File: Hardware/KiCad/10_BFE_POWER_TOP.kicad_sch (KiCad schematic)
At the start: 0 parts

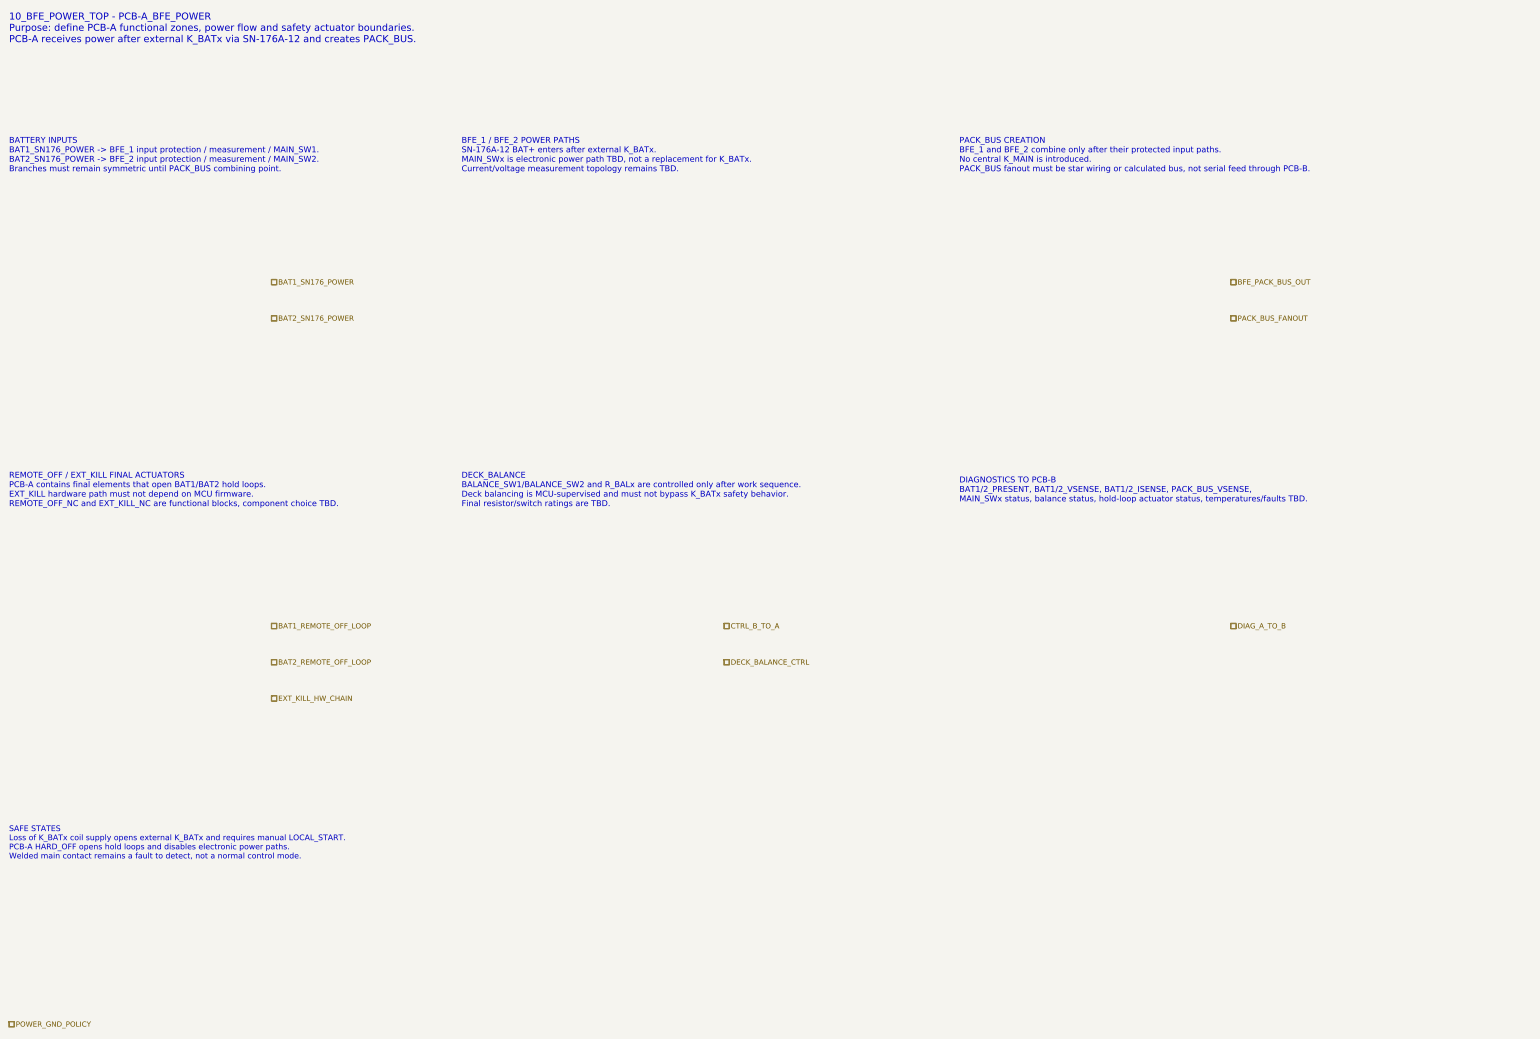
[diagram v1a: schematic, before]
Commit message: hardware: add BFE detailed hierarchy sheets
Add Architecture Level A detailed hierarchy sheets for PCB-A BFE_POWER.

Includes 11_BATTERY_INPUT_1 through 19_BFE_CONNECTORS_TESTPOINTS and updates the BFE top sheet/manifest.

No component selection, footprints, PCB layout, K_MAIN, or .kicad_prl changes.
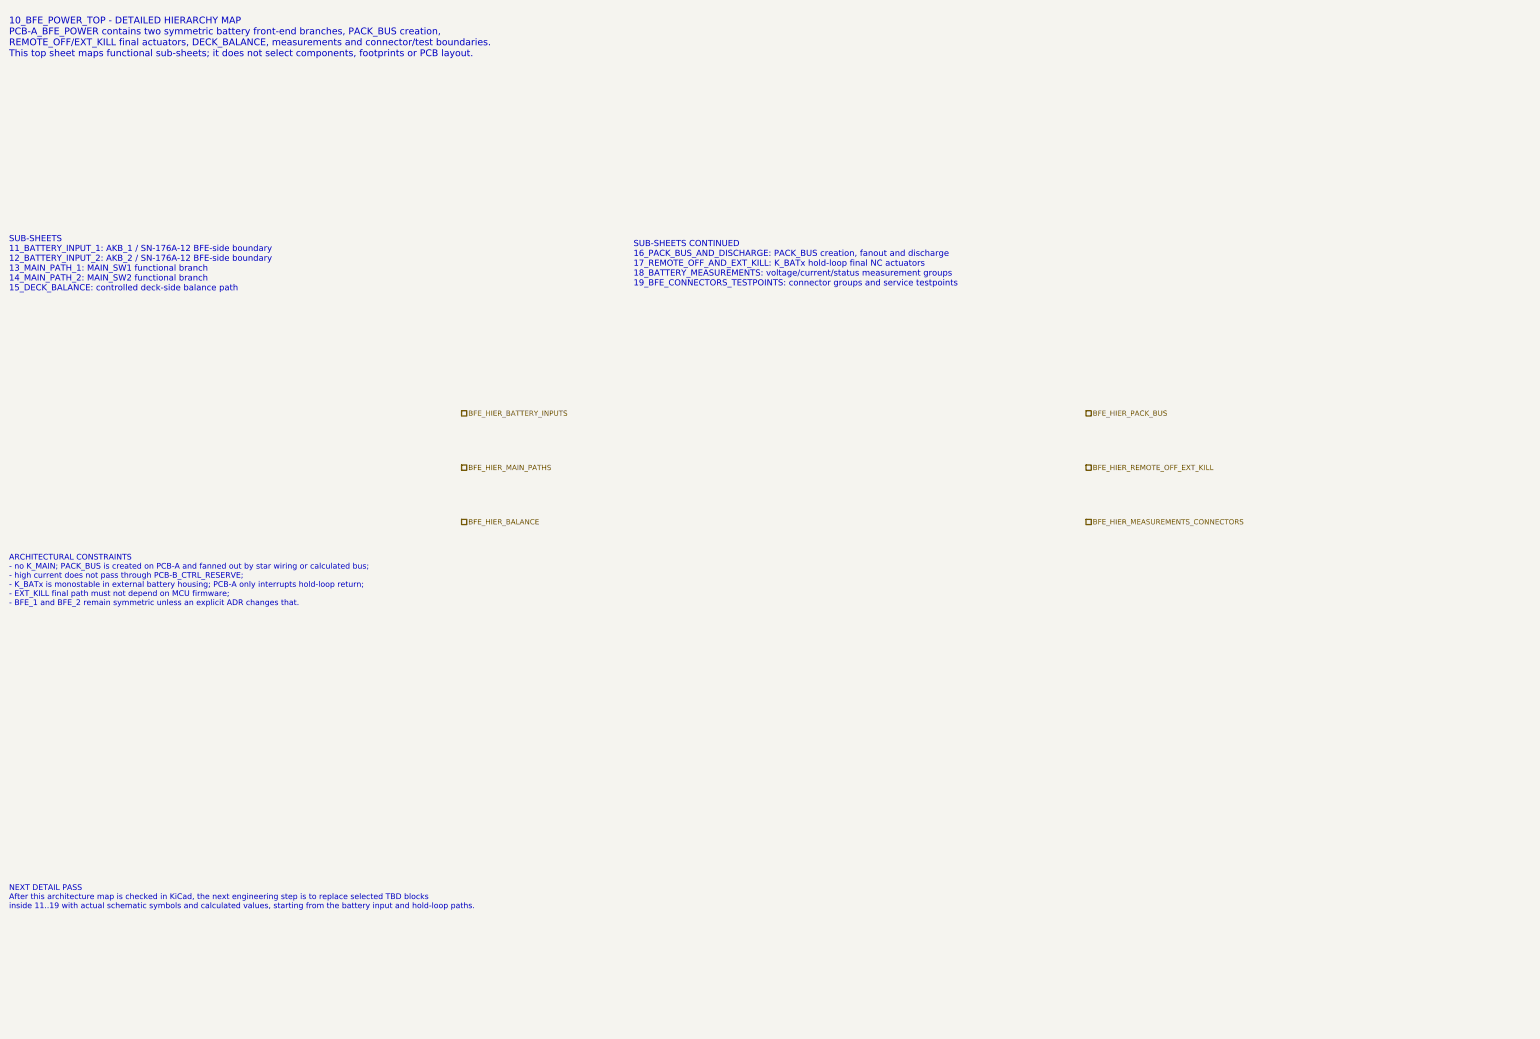
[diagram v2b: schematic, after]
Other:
- note added: "10_BFE_POWER_TOP - DETAILED HIERARCHY MAP PCB-A_BFE_POWER contains two symmetric battery front-end branches, PACK_BUS creation, REMOTE_OFF/EXT_KILL final actuators, DECK_BALANCE, measurements and connector/test boundaries. This top sheet maps functional sub-sheets; it does not select components, footprints or PCB layout."
- note added: "ARCHITECTURAL CONSTRAINTS - no K_MAIN; PACK_BUS is created on PCB-A and fanned out by star wiring or calculated bus; - high current does not pass through PCB-B_CTRL_RESERVE; - K_BATx is monostable in external battery housing; PCB-A only interrupts hold-loop return; - EXT_KILL final path must not depend on MCU firmware; - BFE_1 and BFE_2 remain symmetric unless an explicit ADR changes that."
- note added: "NEXT DETAIL PASS After this architecture map is checked in KiCad, the next engineering step is to replace selected TBD blocks inside 11..19 with actual schematic symbols and calculated values, starting from the battery input and hold-loop paths."
- note added: "SUB-SHEETS 11_BATTERY_INPUT_1: AKB_1 / SN-176A-12 BFE-side boundary 12_BATTERY_INPUT_2: AKB_2 / SN-176A-12 BFE-side boundary 13_MAIN_PATH_1: MAIN_SW1 functional branch 14_MAIN_PATH_2: MAIN_SW2 functional branch 15_DECK_BALANCE: controlled deck-side balance path"
- note added: "SUB-SHEETS CONTINUED 16_PACK_BUS_AND_DISCHARGE: PACK_BUS creation, fanout and discharge 17_REMOTE_OFF_AND_EXT_KILL: K_BATx hold-loop final NC actuators 18_BATTERY_MEASUREMENTS: voltage/current/status measurement groups 19_BFE_CONNECTORS_TESTPOINTS: connector groups and service testpoints"
- note removed: "10_BFE_POWER_TOP - PCB-A_BFE_POWER Purpose: define PCB-A functional zones, power flow and safety actuator boundaries. PCB-A receives power after external K_BATx via SN-176A-12 and creates PACK_BUS."
- note removed: "BATTERY INPUTS BAT1_SN176_POWER -> BFE_1 input protection / measurement / MAIN_SW1. BAT2_SN176_POWER -> BFE_2 input protection / measurement / MAIN_SW2. Branches must remain symmetric until PACK_BUS combining point."
- note removed: "BFE_1 / BFE_2 POWER PATHS SN-176A-12 BAT+ enters after external K_BATx. MAIN_SWx is electronic power path TBD, not a replacement for K_BATx. Current/voltage measurement topology remains TBD."
- note removed: "DECK_BALANCE BALANCE_SW1/BALANCE_SW2 and R_BALx are controlled only after work sequence. Deck balancing is MCU-supervised and must not bypass K_BATx safety behavior. Final resistor/switch ratings are TBD."
- note removed: "DIAGNOSTICS TO PCB-B BAT1/2_PRESENT, BAT1/2_VSENSE, BAT1/2_ISENSE, PACK_BUS_VSENSE, MAIN_SWx status, balance status, hold-loop actuator status, temperatures/faults TBD."
- note removed: "PACK_BUS CREATION BFE_1 and BFE_2 combine only after their protected input paths. No central K_MAIN is introduced. PACK_BUS fanout must be star wiring or calculated bus, not serial feed through PCB-B."
- note removed: "REMOTE_OFF / EXT_KILL FINAL ACTUATORS PCB-A contains final elements that open BAT1/BAT2 hold loops. EXT_KILL hardware path must not depend on MCU firmware. REMOTE_OFF_NC and EXT_KILL_NC are functional blocks, component choice TBD."
- note removed: "SAFE STATES Loss of K_BATx coil supply opens external K_BATx and requires manual LOCAL_START. PCB-A HARD_OFF opens hold loops and disables electronic power paths. Welded main contact remains a fault to detect, not a normal control mode."
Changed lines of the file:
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@@
 		(title "10_BFE_POWER_TOP - PCB-A_BFE_POWER")
 		(date "2026-07-15")
-		(rev "A1")
+		(rev "A2")
 		(company "Gonoboben/plataVM")
-		(comment 1 "Architecture Level A: BFE branches, PACK_BUS and final HARD_OFF actuators")
-		(comment 2 "No K_BATx/MAIN_SWx/current sensor part numbers selected")
+		(comment 1 "Architecture Level A: BFE detailed hierarchy map")
+		(comment 2 "Sub-sheets 11..19 define functional boundaries only")
 	)
-	(text "10_BFE_POWER_TOP - PCB-A_BFE_POWER\nPurpose: define PCB-A functional zones, power flow and safety actuator boundaries.\nPCB-A receives power after external K_BATx via SN-176A-12 and creates PACK_BUS."
+	(text "10_BFE_POWER_TOP - DETAILED HIERARCHY MAP\nPCB-A_BFE_POWER contains two symmetric battery front-end branches, PACK_BUS creation,\nREMOTE_OFF/EXT_KILL final actuators, DECK_BALANCE, measurements and connector/test boundaries.\nThis top sheet maps functional sub-sheets; it does not select components, footprints or PCB layout."
 		(exclude_from_sim no)
-		(at 12 10 0)
-		(effects (font (size 1.55 1.55)) (justify left))
-		(uuid "bfe-a-text-0001")
+		(at 12 12 0)
+		(effects (font (size 1.5 1.5)) (justify left))
+		(uuid "bfe-top-00000010-0000-4000-8000-000000000101")
 	)
-	(text "BATTERY INPUTS\nBAT1_SN176_POWER -> BFE_1 input protection / measurement / MAIN_SW1.\nBAT2_SN176_POWER -> BFE_2 input protection / measurement / MAIN_SW2.\nBranches must remain symmetric until PACK_BUS combining point."
+	(text "SUB-SHEETS\n11_BATTERY_INPUT_1: AKB_1 / SN-176A-12 BFE-side boundary\n12_BATTERY_INPUT_2: AKB_2 / SN-176A-12 BFE-side boundary\n13_MAIN_PATH_1: MAIN_SW1 functional branch\n14_MAIN_PATH_2: MAIN_SW2 functional branch\n15_DECK_BALANCE: controlled deck-side balance path"
 		(exclude_from_sim no)
-		(at 12 38 0)
-		(effects (font (size 1.3 1.3)) (justify left))
-		(uuid "bfe-a-text-0002")
+		(at 12 62 0)
+		(effects (font (size 1.35 1.35)) (justify left))
+		(uuid "bfe-top-00000010-0000-4000-8000-000000000102")
 	)
-	(text "BFE_1 / BFE_2 POWER PATHS\nSN-176A-12 BAT+ enters after external K_BATx.\nMAIN_SWx is electronic power path TBD, not a replacement for K_BATx.\nCurrent/voltage measurement topology remains TBD."
+	(text "SUB-SHEETS CONTINUED\n16_PACK_BUS_AND_DISCHARGE: PACK_BUS creation, fanout and discharge\n17_REMOTE_OFF_AND_EXT_KILL: K_BATx hold-loop final NC actuators\n18_BATTERY_MEASUREMENTS: voltage/current/status measurement groups\n19_BFE_CONNECTORS_TESTPOINTS: connector groups and service testpoints"
 		(exclude_from_sim no)
-		(at 112 38 0)
-		(effects (font (size 1.3 1.3)) (justify left))
-		(uuid "bfe-a-text-0003")
+		(at 150 62 0)
+		(effects (font (size 1.35 1.35)) (justify left))
+		(uuid "bfe-top-00000010-0000-4000-8000-000000000103")
 	)
-	(text "PACK_BUS CREATION\nBFE_1 and BFE_2 combine only after their protected input paths.\nNo central K_MAIN is introduced.\nPACK_BUS fanout must be star wiring or calculated bus, not serial feed through PCB-B."
+	(text "ARCHITECTURAL CONSTRAINTS\n- no K_MAIN; PACK_BUS is created on PCB-A and fanned out by star wiring or calculated bus;\n- high current does not pass through PCB-B_CTRL_RESERVE;\n- K_BATx is monostable in external battery housing; PCB-A only interrupts hold-loop return;\n- EXT_KILL final path must not depend on MCU firmware;\n- BFE_1 and BFE_2 remain symmetric unless an explicit ADR changes that."
 		(exclude_from_sim no)
-		(at 222 38 0)
-		(effects (font (size 1.3 1.3)) (justify left))
-		(uuid "bfe-a-text-0004")
+		(at 12 132 0)
+		(effects (font (size 1.25 1.25)) (justify left))
+		(uuid "bfe-top-00000010-0000-4000-8000-000000000104")
 	)
-	(text "REMOTE_OFF / EXT_KILL FINAL ACTUATORS\nPCB-A contains final elements that open BAT1/BAT2 hold loops.\nEXT_KILL hardware path must not depend on MCU firmware.\nREMOTE_OFF_NC and EXT_KILL_NC are functional blocks, component choice TBD."
+	(text "NEXT DETAIL PASS\nAfter this architecture map is checked in KiCad, the next engineering step is to replace selected TBD blocks\ninside 11..19 with actual schematic symbols and calculated values, starting from the battery input and hold-loop paths."
 		(exclude_from_sim no)
-		(at 12 112 0)
-		(effects (font (size 1.3 1.3)) (justify left))
-		(uuid "bfe-a-text-0005")
+		(at 12 202 0)
+		(effects (font (size 1.25 1.25)) (justify left))
+		(uuid "bfe-top-00000010-0000-4000-8000-000000000105")
 	)
-	(text "DECK_BALANCE\nBALANCE_SW1/BALANCE_SW2 and R_BALx are controlled only after work sequence.\nDeck balancing is MCU-supervised and must not bypass K_BATx safety behavior.\nFinal resistor/switch ratings are TBD."
-		(exclude_from_sim no)
-		(at 112 112 0)
-		(effects (font (size 1.3 1.3)) (justify left))
-		(uuid "bfe-a-text-0006")
-	)
-	(text "DIAGNOSTICS TO PCB-B\nBAT1/2_PRESENT, BAT1/2_VSENSE, BAT1/2_ISENSE, PACK_BUS_VSENSE,\nMAIN_SWx status, balance status, hold-loop actuator status, temperatures/faults TBD."
-		(exclude_from_sim no)
-		(at 222 112 0)
-		(effects (font (size 1.3 1.3)) (justify left))
-		(uuid "bfe-a-text-0007")
-	)
-	(text "SAFE STATES\nLoss of K_BATx coil supply opens external K_BATx and requires manual LOCAL_START.\nPCB-A HARD_OFF opens hold loops and disables electronic power paths.\nWelded main contact remains a fault to detect, not a normal control mode."
-		(exclude_from_sim no)
-		(at 12 190 0)
-		(effects (font (size 1.25 1.25)) (justify left))
-		(uuid "bfe-a-text-0008")
-	)
-	(hierarchical_label "BAT1_SN176_POWER" (shape passive) (exclude_from_sim no) (at 70 66 0) (effects (font (size 1.15 1.15)) (justify left)) (uuid "bfe-a-label-0001"))
-	(hierarchical_label "BAT2_SN176_POWER" (shape passive) (exclude_from_sim no) (at 70 74 0) (effects (font (size 1.15 1.15)) (justify left)) (uuid "bfe-a-label-0002"))
-	(hierarchical_label "BAT1_REMOTE_OFF_LOOP" (shape passive) (exclude_from_sim no) (at 70 142 0) (effects (font (size 1.15 1.15)) (justify left)) (uuid "bfe-a-label-0003"))
-	(hierarchical_label "BAT2_REMOTE_OFF_LOOP" (shape passive) (exclude_from_sim no) (at 70 150 0) (effects (font (size 1.15 1.15)) (justify left)) (uuid "bfe-a-label-0004"))
-	(hierarchical_label "EXT_KILL_HW_CHAIN" (shape passive) (exclude_from_sim no) (at 70 158 0) (effects (font (size 1.15 1.15)) (justify left)) (uuid "bfe-a-label-0005"))
-	(hierarchical_label "BFE_PACK_BUS_OUT" (shape passive) (exclude_from_sim no) (at 282 66 0) (effects (font (size 1.15 1.15)) (justify left)) (uuid "bfe-a-label-0006"))
-	(hierarchical_label "PACK_BUS_FANOUT" (shape passive) (exclude_from_sim no) (at 282 74 0) (effects (font (size 1.15 1.15)) (justify left)) (uuid "bfe-a-label-0007"))
-	(hierarchical_label "CTRL_B_TO_A" (shape passive) (exclude_from_sim no) (at 170 142 0) (effects (font (size 1.15 1.15)) (justify left)) (uuid "bfe-a-label-0008"))
-	(hierarchical_label "DIAG_A_TO_B" (shape passive) (exclude_from_sim no) (at 282 142 0) (effects (font (size 1.15 1.15)) (justify left)) (uuid "bfe-a-label-0009"))
-	(hierarchical_label "DECK_BALANCE_CTRL" (shape passive) (exclude_from_sim no) (at 170 150 0) (effects (font (size 1.15 1.15)) (justify left)) (uuid "bfe-a-label-0010"))
-	(hierarchical_label "POWER_GND_POLICY" (shape passive) (exclude_from_sim no) (at 12 230 0) (effects (font (size 1.15 1.15)) (justify left)) (uuid "bfe-a-label-0011"))
+	(hierarchical_label "BFE_HIER_BATTERY_INPUTS" (shape passive) (exclude_from_sim no) (at 112 95 0) (effects (font (size 1.15 1.15)) (justify left)) (uuid "bfe-top-00000010-0000-4000-8000-000000000201"))
+	(hierarchical_label "BFE_HIER_MAIN_PATHS" (shape passive) (exclude_from_sim no) (at 112 107 0) (effects (font (size 1.15 1.15)) (justify left)) (uuid "bfe-top-00000010-0000-4000-8000-000000000202"))
+	(hierarchical_label "BFE_HIER_BALANCE" (shape passive) (exclude_from_sim no) (at 112 119 0) (effects (font (size 1.15 1.15)) (justify left)) (uuid "bfe-top-00000010-0000-4000-8000-000000000203"))
+	(hierarchical_label "BFE_HIER_PACK_BUS" (shape passive) (exclude_from_sim no) (at 250 95 0) (effects (font (size 1.15 1.15)) (justify left)) (uuid "bfe-top-00000010-0000-4000-8000-000000000204"))
+	(hierarchical_label "BFE_HIER_REMOTE_OFF_EXT_KILL" (shape passive) (exclude_from_sim no) (at 250 107 0) (effects (font (size 1.15 1.15)) (justify left)) (uuid "bfe-top-00000010-0000-4000-8000-000000000205"))
+	(hierarchical_label "BFE_HIER_MEASUREMENTS_CONNECTORS" (shape passive) (exclude_from_sim no) (at 250 119 0) (effects (font (size 1.15 1.15)) (justify left)) (uuid "bfe-top-00000010-0000-4000-8000-000000000206"))
 )
